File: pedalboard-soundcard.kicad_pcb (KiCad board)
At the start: 2 copper layers, 65 x 56 mm, 91 parts, among them J1 RPi_GPIO, J2 Conn_02x03_Odd_Even, J3 Conn_02x03_Odd_Even, J4 Audio_Jack, J5 Audio_Jack, T1 Tab, T2 Tab, T3 Tab, T4 Tab, U1 AT24CS01-STUM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

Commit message: Add first pnp job
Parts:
- C1, C11, C14, C16, C19, C20, C28, C29, C32: value 100nF25V -> 100n
- C10, C12, C15, C2, C3, C4, C5, C6, C7, C8, C9: value 10uF16V -> 10u
- C13, C17, C18, C23, C24, C27, C30, C31: value 1uF16V -> 1u
- C21, C22, C25, C26: value 2,2nF50V -> 2n2
- C33, C34: value 10nF -> 10n_film
- D1, D2: value LED -> red
- X1: value 22.5792Mhz -> 22.5792M
- X2: value 24.576Mhz -> 24.576M
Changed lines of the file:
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@@
 			)
 		)
-		(property "Value" "2,2nF50V"
+		(property "Value" "2n2"
 			(at 0 1.68 90)
 			(layer "F.Fab")
@@
 			)
 		)
-		(property "Value" "22.5792Mhz"
+		(property "Value" "22.5792M"
 			(at 0 2.45 90)
 			(layer "F.Fab")
@@
 			)
 		)
-		(property "Value" "10uF16V"
+		(property "Value" "10u"
 			(at 0 1.68 90)
 			(layer "F.Fab")
@@
 			)
 		)
-		(property "Value" "100nF25V"
+		(property "Value" "100n"
 			(at 0 1.68 90)
 			(layer "F.Fab")
@@
 			)
 		)
-		(property "Value" "100nF25V"
+		(property "Value" "100n"
 			(at 0 1.68 0)
 			(layer "F.Fab")
@@
 			)
 		)
-		(property "Value" "24.576Mhz"
+		(property "Value" "24.576M"
 			(at 0 2.45 90)
 			(layer "F.Fab")
@@
 			)
 		)
-		(property "Value" "LED"
+		(property "Value" "red"
 			(at 0 1.65 90)
 			(layer "F.Fab")
@@
 			)
 		)
-		(property "Value" "100nF25V"
+		(property "Value" "100n"
 			(at 0 1.68 90)
 			(layer "F.Fab")
@@
 			)
 		)
-		(property "Value" "100nF25V"
+		(property "Value" "100n"
 			(at 0 1.68 0)
 			(layer "F.Fab")
@@
 			)
 		)
-		(property "Value" "100nF25V"
+		(property "Value" "100n"
 			(at 0 1.68 0)
 			(layer "F.Fab")
@@
 			)
 		)
-		(property "Value" "10uF16V"
+		(property "Value" "10u"
 			(at 0 1.68 90)
 			(layer "F.Fab")
@@
 			)
 		)
-		(property "Value" "10uF16V"
+		(property "Value" "10u"
 			(at 0 1.68 90)
 			(layer "F.Fab")
@@
 			)
 		)
-		(property "Value" "1uF16V"
+		(property "Value" "1u"
 			(at 0 1.68 90)
 			(layer "F.Fab")
@@
 			)
 		)
-		(property "Value" "10uF16V"
+		(property "Value" "10u"
 			(at 0 1.68 0)
 			(layer "F.Fab")
@@
 			)
 		)
-		(property "Value" "1uF16V"
+		(property "Value" "1u"
 			(at 0 1.68 0)
 			(layer "F.Fab")
@@
 			)
 		)
-		(property "Value" "10uF16V"
+		(property "Value" "10u"
 			(at 0 1.68 0)
 			(layer "F.Fab")
@@
 			)
 		)
-		(property "Value" "2,2nF50V"
+		(property "Value" "2n2"
 			(at 0 1.68 90)
 			(layer "F.Fab")
@@
 			)
 		)
-		(property "Value" "10uF16V"
+		(property "Value" "10u"
 			(at 0 1.68 0)
 			(layer "F.Fab")
@@
 			)
 		)
-		(property "Value" "1uF16V"
+		(property "Value" "1u"
 			(at 0 1.68 90)
 			(layer "F.Fab")
@@
 			)
 		)
-		(property "Value" "10uF16V"
+		(property "Value" "10u"
 			(at 0 1.68 0)
 			(layer "F.Fab")
@@
 			)
 		)
-		(property "Value" "1uF16V"
+		(property "Value" "1u"
 			(at 0 1.68 0)
 			(layer "F.Fab")
@@
 			)
 		)
-		(property "Value" "2,2nF50V"
+		(property "Value" "2n2"
 			(at 0 1.68 90)
 			(layer "F.Fab")
@@
 			)
 		)
-		(property "Value" "1uF16V"
+		(property "Value" "1u"
 			(at 0 1.68 0)
 			(layer "F.Fab")
@@
 			)
 		)
-		(property "Value" "LED"
+		(property "Value" "red"
 			(at 0 1.65 0)
 			(layer "F.Fab")
@@
 			)
 		)
-		(property "Value" "10uF16V"
+		(property "Value" "10u"
 			(at 0 1.68 0)
 			(layer "F.Fab")
@@
 			)
 		)
-		(property "Value" "10nF"
+		(property "Value" "10n_film"
 			(at 0 1.68 0)
 			(layer "F.Fab")
@@
 			)
 		)
-		(property "Value" "10uF16V"
+		(property "Value" "10u"
 			(at 0 1.68 0)
 			(layer "F.Fab")
@@
 			)
 		)
-		(property "Value" "2,2nF50V"
+		(property "Value" "2n2"
 			(at 0 1.68 90)
 			(layer "F.Fab")
@@
 			)
 		)
-		(property "Value" "1uF16V"
+		(property "Value" "1u"
 			(at 0 1.68 90)
 			(layer "F.Fab")
@@
 			)
 		)
-		(property "Value" "100nF25V"
+		(property "Value" "100n"
 			(at 0 1.68 0)
 			(layer "F.Fab")
@@
 			)
 		)
-		(property "Value" "100nF25V"
+		(property "Value" "100n"
 			(at 0 1.68 90)
 			(layer "F.Fab")
@@
 			)
 		)
-		(property "Value" "10nF"
+		(property "Value" "10n_film"
 			(at 0 1.68 0)
 			(layer "F.Fab")
@@
 			)
 		)
-		(property "Value" "100nF25V"
+		(property "Value" "100n"
 			(at 0 1.68 90)
 			(layer "F.Fab")
@@
 			)
 		)
-		(property "Value" "10uF16V"
+		(property "Value" "10u"
 			(at 0 1.68 0)
 			(layer "F.Fab")
@@
 			)
 		)
-		(property "Value" "1uF16V"
+		(property "Value" "1u"
 			(at 0 1.68 0)
 			(layer "F.Fab")
@@
 			)
 		)
-		(property "Value" "100nF25V"
+		(property "Value" "100n"
 			(at 0 1.68 0)
 			(layer "F.Fab")
@@
 			)
 		)
-		(property "Value" "10uF16V"
+		(property "Value" "10u"
 			(at 0 1.68 90)
 			(layer "F.Fab")
@@
 			)
 		)
-		(property "Value" "1uF16V"
+		(property "Value" "1u"
 			(at 0 1.68 90)
 			(layer "F.Fab")

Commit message: Align LED value with other projects
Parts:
- D1, D2: value red -> LED_R
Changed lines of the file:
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@@
 			)
 		)
-		(property "Value" "red"
+		(property "Value" "LED_R"
 			(at 0 1.65 90)
 			(layer "F.Fab")
@@
 			)
 		)
-		(property "Value" "red"
+		(property "Value" "LED_R"
 			(at 0 1.65 0)
 			(layer "F.Fab")

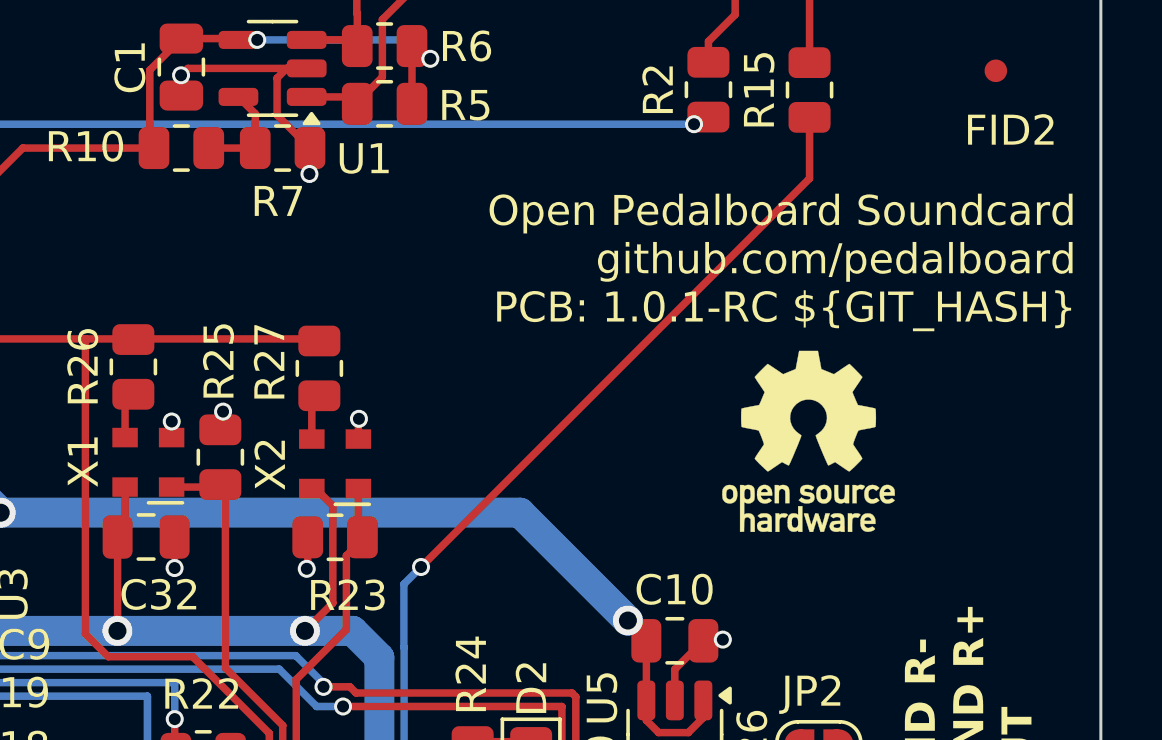
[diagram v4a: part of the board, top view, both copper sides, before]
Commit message: Fix all DRC errors
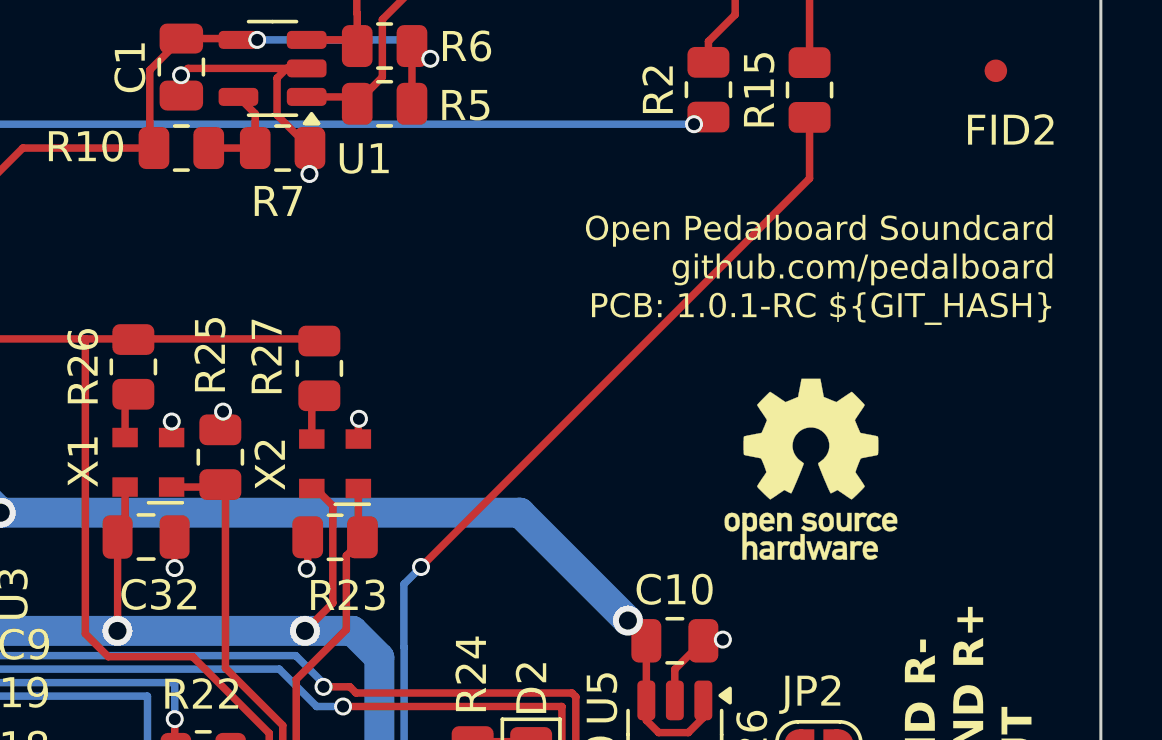
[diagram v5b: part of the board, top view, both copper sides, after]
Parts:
- moved SYM1 0.93 mm to (103.8, 74.3)
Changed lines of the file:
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@@
 		(tags "resistor")
 		(property "Reference" "R25"
-			(at 3.2 -0.025 90)
+			(at 3.41 -0.31 90)
 			(layer "F.SilkS")
 			(effects
@@
 		(layer "F.Cu")
 		(at 67.4 63.85 -90)
-		(descr "SOT, 5 Pin (https://www.jedec.org/sites/default/files/docs/Mo-178c.PDF variant AA), generated with kicad-footprint-generator ipc_gullwing_generator.py")
+		(descr "SOT, 5 Pin (~), generated with kicad-footprint-generator ipc_gullwing_generator.py")
 		(tags "SOT TO_SOT_SMD")
 		(property "Reference" "U2"
@@
 	(footprint "Symbol:OSHW-Logo_5.7x6mm_SilkScreen"
 		(layer "F.Cu")
-		(at 103.75 73.35)
+		(at 103.83 74.28)
 		(descr "Open Source Hardware Logo")
 		(tags "Logo OSHW")
@@
 		(layer "F.Cu")
 		(at 99.3 83.125 -90)
-		(descr "SOT, 5 Pin (https://www.jedec.org/sites/default/files/docs/Mo-178c.PDF variant AA), generated with kicad-footprint-generator ipc_gullwing_generator.py")
+		(descr "SOT, 5 Pin (~), generated with kicad-footprint-generator ipc_gullwing_generator.py")
 		(tags "SOT TO_SOT_SMD")
 		(property "Reference" "U5"
@@
 		(layer "F.Cu")
 		(at 74.85 78.45 -90)
-		(descr "SOT, 5 Pin (https://www.jedec.org/sites/default/files/docs/Mo-178c.PDF variant AA), generated with kicad-footprint-generator ipc_gullwing_generator.py")
+		(descr "SOT, 5 Pin (~), generated with kicad-footprint-generator ipc_gullwing_generator.py")
 		(tags "SOT TO_SOT_SMD")
 		(property "Reference" "U3"
@@
 		(tags "resistor")
 		(property "Reference" "R27"
-			(at 0.21 -1.63 90)
+			(at 0.39 -1.72 90)
 			(layer "F.SilkS")
 			(effects
@@
 		(layer "F.Cu")
 		(at 85.89 60.92 180)
-		(descr "SOT, 5 Pin (https://www.jedec.org/sites/default/files/docs/Mo-178c.PDF variant AA), generated with kicad-footprint-generator ipc_gullwing_generator.py")
+		(descr "SOT, 5 Pin (~), generated with kicad-footprint-generator ipc_gullwing_generator.py")
 		(tags "SOT TO_SOT_SMD")
 		(property "Reference" "U1"
@@
 	)
 	(gr_text "${TITLE}\n${COMPANY}\nPCB: ${REVISION} ${GIT_HASH}"
-		(at 112.55 69.54 0)
+		(at 111.72 69.34 0)
 		(layer "B.SilkS")
 		(effects
 			(font
-				(size 1 1)
+				(size 0.8 0.8)
 				(thickness 0.15)
 			)
@@
 	)
 	(gr_text "${TITLE}\n${COMPANY}\nPCB: ${REVISION} ${GIT_HASH}"
-		(at 112.68 69.48 0)
+		(at 111.98 69.31 0)
 		(layer "F.SilkS")
 		(effects
 			(font
-				(size 1 1)
+				(size 0.8 0.8)
 				(thickness 0.15)
 			)
